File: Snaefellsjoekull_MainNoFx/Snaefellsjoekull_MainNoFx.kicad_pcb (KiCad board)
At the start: 2 copper layers, 43.2 x 81.3 mm, 28 parts, among them J1 Eurorack Power, J2 Bus Connector, J3 Right Out, J4 Left Out, U1 TL072, U2 TL072

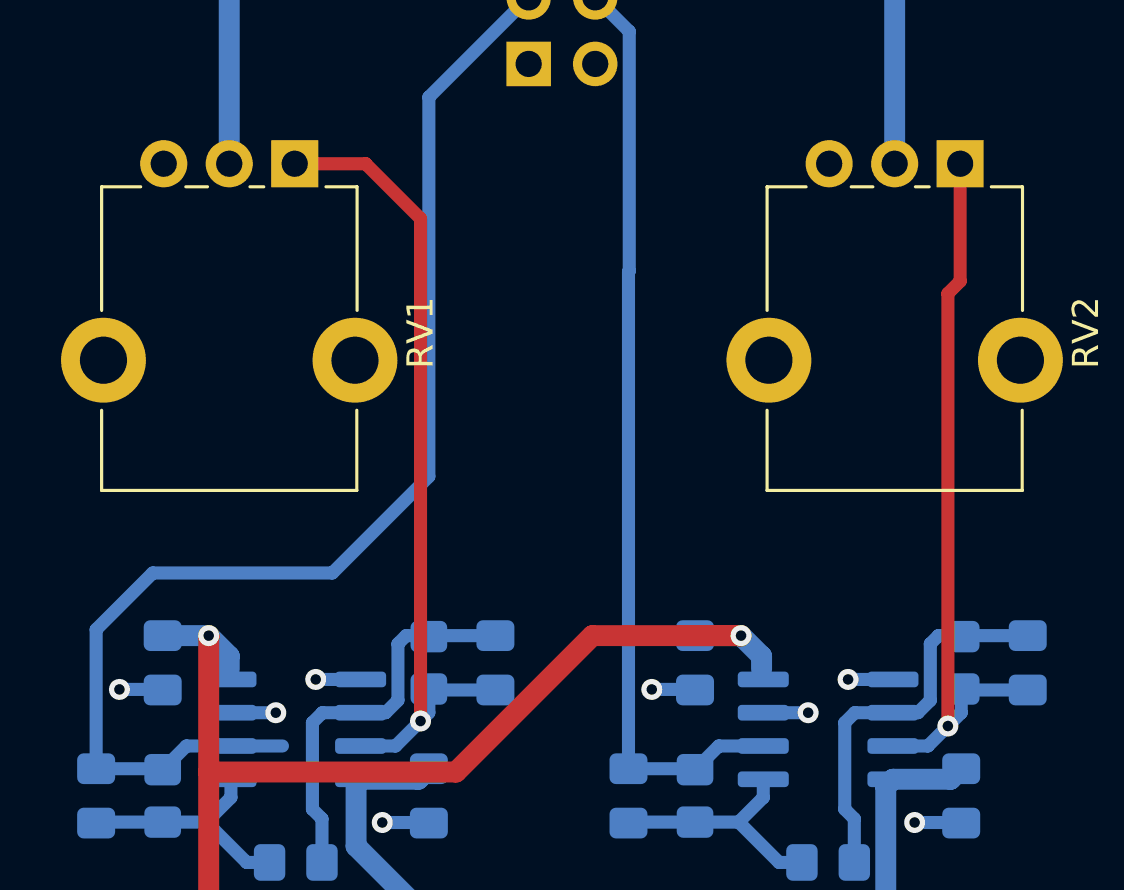
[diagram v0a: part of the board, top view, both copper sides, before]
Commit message: Potentiometer fixed
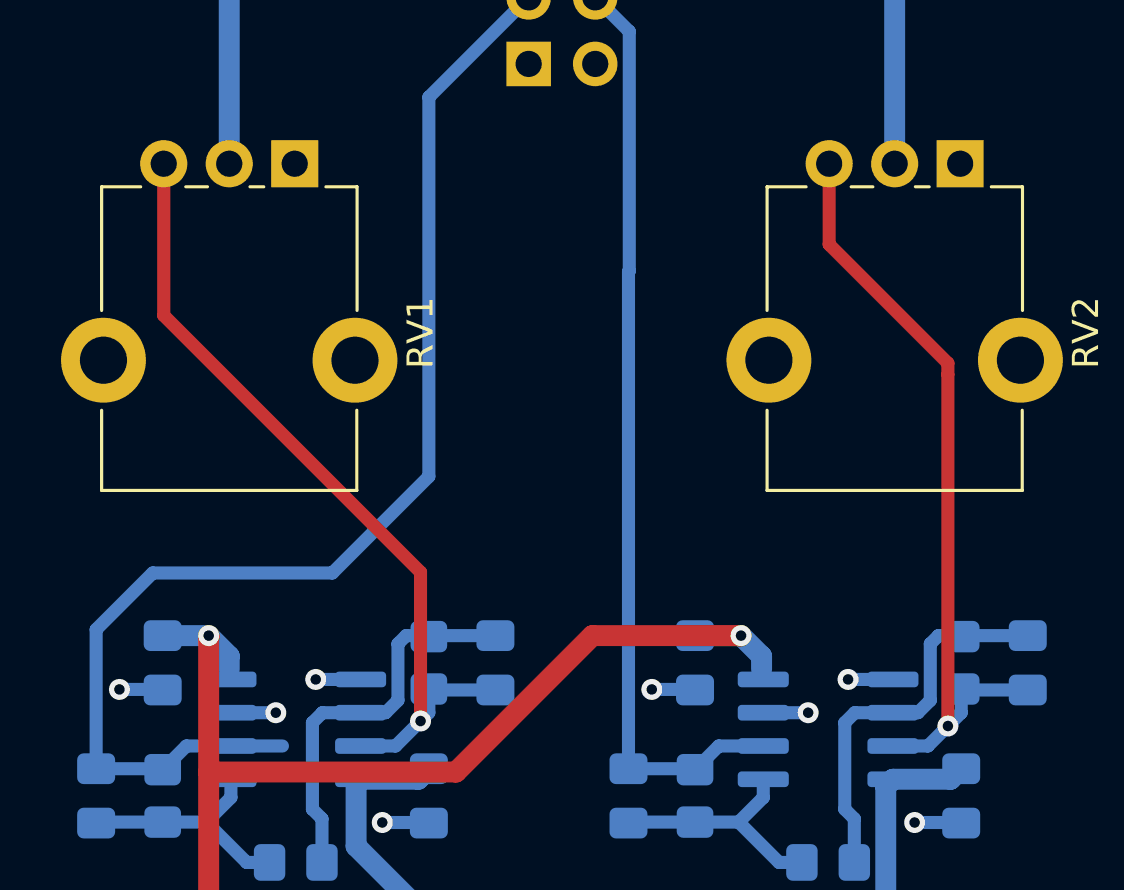
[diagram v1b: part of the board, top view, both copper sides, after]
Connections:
- RV1 pad 1: Net-(C7-Pad2) -> GND
- RV1 pad 3: GND -> Net-(C7-Pad2)
- RV2 pad 1: Net-(C8-Pad2) -> GND
- RV2 pad 3: GND -> Net-(C8-Pad2)
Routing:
- net Net-(C8-Pad2): track 28.2 -> 29.9 mm
